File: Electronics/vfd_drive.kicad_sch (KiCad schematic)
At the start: 3 parts, among them J6 Conn_01x08_Pin, U3 74HC595, U4 TBD62783A

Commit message: Added filament timer
Added a timer to control the filament h-brdige on the main PCB.
Also added some more decoupling capacitors, but some have dubious
placement. Still better than nothing.
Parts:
- added C13: 100n, Capacitor_THT:C_Disc_D5.1mm_W3.2mm_P5.00mm, symbol Device:C
- renumbered U3 to U4, U4 to U5
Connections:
- net GND: now also C13.2
- net LOGIC_VCC: now also C13.1
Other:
- note added: "Decoupling"

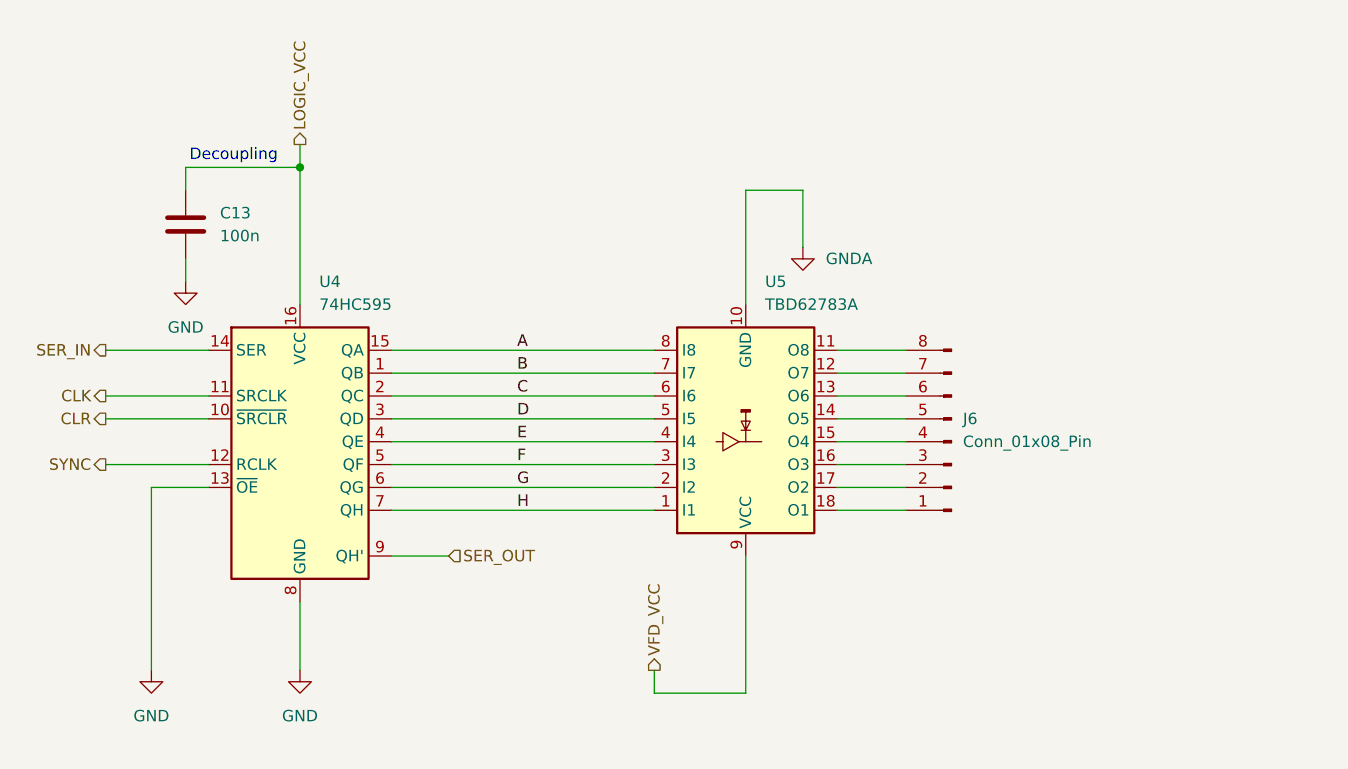
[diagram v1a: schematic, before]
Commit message: Added VFD output pulldowns
Added pulldowns and more decoupling capacitors. The capacitors and
pulldowns can probably be omitted, but I've put them in for more flexibility.
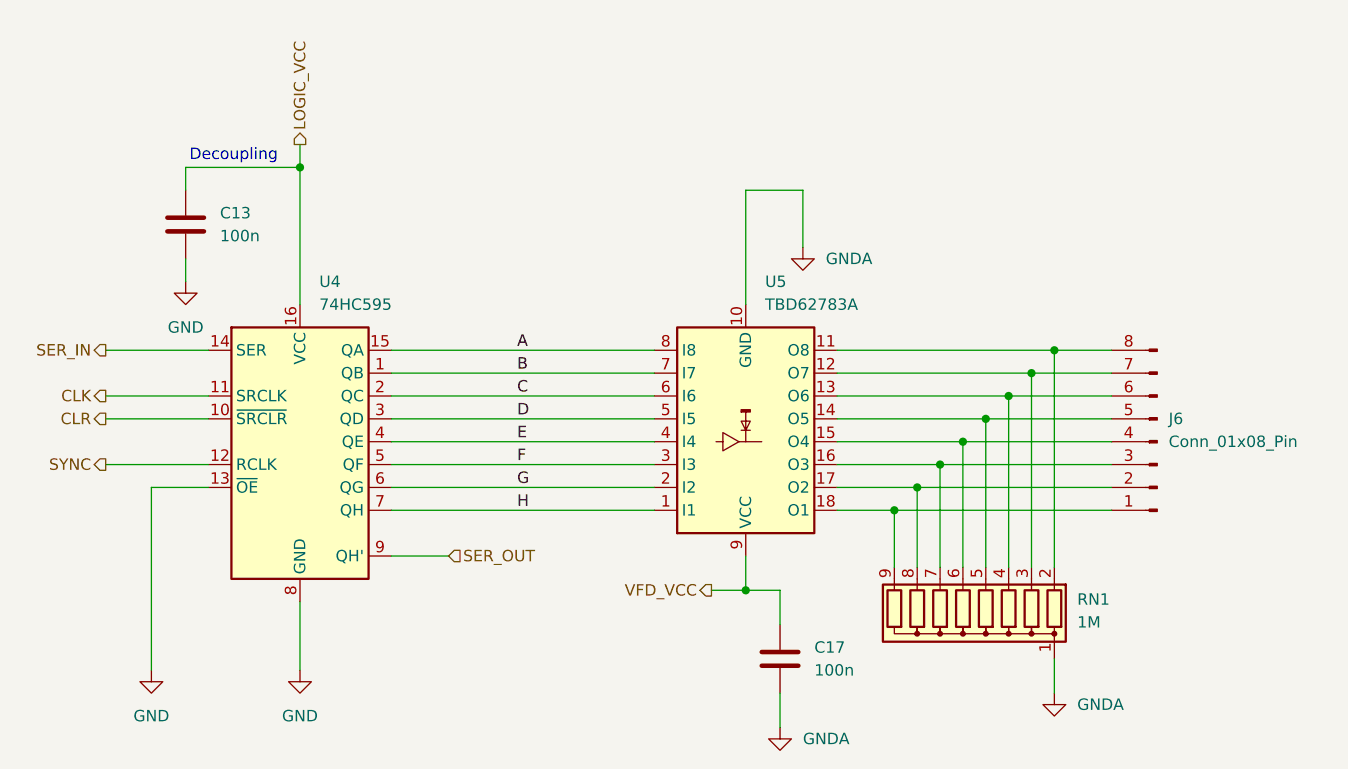
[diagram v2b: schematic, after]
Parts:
- added C17: 100n, Capacitor_THT:C_Disc_D5.1mm_W3.2mm_P5.00mm, symbol Device:C
- added RN1: 1M, Resistor_THT:R_Array_SIP9, symbol Device:R_Network08
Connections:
- net GNDA: now also C17.2, RN1.1 (common)
- net VFD_VCC: now also C17.1
- net at J6.8 (Pin_8), U5.11 (O8): now also RN1.2 (R1)
- net at J6.7 (Pin_7), U5.12 (O7): now also RN1.3 (R2)
- net at J6.6 (Pin_6), U5.13 (O6): now also RN1.4 (R3)
- net at J6.5 (Pin_5), U5.14 (O5): now also RN1.5 (R4)
- net at J6.4 (Pin_4), U5.15 (O4): now also RN1.6 (R5)
- net at J6.3 (Pin_3), U5.16 (O3): now also RN1.7 (R6)
- net at J6.2 (Pin_2), U5.17 (O2): now also RN1.8 (R7)
- net at J6.1 (Pin_1), U5.18 (O1): now also RN1.9 (R8)
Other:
- moved on the sheet: J6

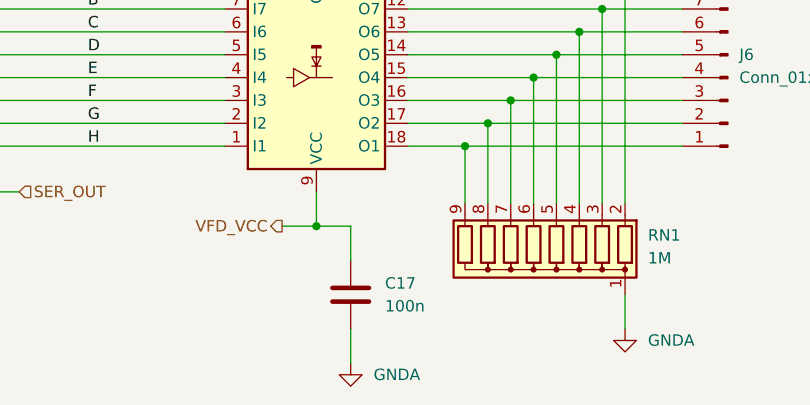
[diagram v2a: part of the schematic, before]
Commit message: Fixed H-bridge
Old H-bridge was the wrong type, changed to using some P-channel
mosfets. Also fixed the cost spreadsheet.
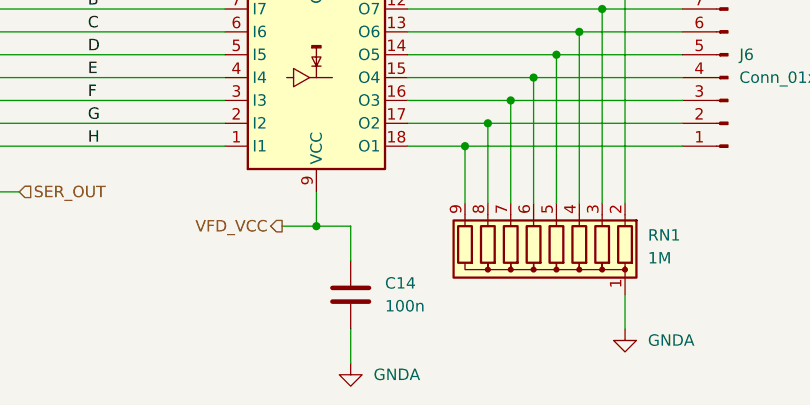
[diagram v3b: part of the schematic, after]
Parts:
- renumbered C17 to C14
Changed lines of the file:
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@@
 			(project "vfd"
 				(path "/36e0811c-69c7-4576-98bb-165d7651c83d/27d484a1-8c30-4726-b590-26be001e1b89"
-					(reference "#PWR082")
-					(unit 1)
-				)
-				(path "/36e0811c-69c7-4576-98bb-165d7651c83d/4abe82bf-2397-47f3-bdf5-0f85616bed30"
 					(reference "#PWR086")
 					(unit 1)
 				)
+				(path "/36e0811c-69c7-4576-98bb-165d7651c83d/4abe82bf-2397-47f3-bdf5-0f85616bed30"
+					(reference "#PWR092")
+					(unit 1)
+				)
 				(path "/36e0811c-69c7-4576-98bb-165d7651c83d/64881d92-68ba-4505-901e-5a279b3a305e"
 					(reference "#PWR074")
@@
 				)
 				(path "/36e0811c-69c7-4576-98bb-165d7651c83d/dcab1e90-0fd0-4de9-948e-22e325fd164f"
-					(reference "#PWR078")
+					(reference "#PWR080")
 					(unit 1)
 				)
@@
 			(project "vfd"
 				(path "/36e0811c-69c7-4576-98bb-165d7651c83d/27d484a1-8c30-4726-b590-26be001e1b89"
-					(reference "#PWR085")
-					(unit 1)
-				)
-				(path "/36e0811c-69c7-4576-98bb-165d7651c83d/4abe82bf-2397-47f3-bdf5-0f85616bed30"
 					(reference "#PWR089")
 					(unit 1)
 				)
+				(path "/36e0811c-69c7-4576-98bb-165d7651c83d/4abe82bf-2397-47f3-bdf5-0f85616bed30"
+					(reference "#PWR095")
+					(unit 1)
+				)
 				(path "/36e0811c-69c7-4576-98bb-165d7651c83d/64881d92-68ba-4505-901e-5a279b3a305e"
 					(reference "#PWR077")
@@
 				)
 				(path "/36e0811c-69c7-4576-98bb-165d7651c83d/dcab1e90-0fd0-4de9-948e-22e325fd164f"
-					(reference "#PWR081")
+					(reference "#PWR083")
 					(unit 1)
 				)
@@
 		(dnp no)
 		(fields_autoplaced yes)
-		(property "Reference" "#PWR090"
+		(property "Reference" "#PWR078"
 			(at 162.56 92.71 0)
 			(effects
@@
 			(project "vvfd"
 				(path "/36e0811c-69c7-4576-98bb-165d7651c83d/27d484a1-8c30-4726-b590-26be001e1b89"
-					(reference "#PWR092")
-					(unit 1)
-				)
-				(path "/36e0811c-69c7-4576-98bb-165d7651c83d/4abe82bf-2397-47f3-bdf5-0f85616bed30"
-					(reference "#PWR093")
-					(unit 1)
-				)
-				(path "/36e0811c-69c7-4576-98bb-165d7651c83d/64881d92-68ba-4505-901e-5a279b3a305e"
 					(reference "#PWR090")
 					(unit 1)
 				)
-				(path "/36e0811c-69c7-4576-98bb-165d7651c83d/dcab1e90-0fd0-4de9-948e-22e325fd164f"
-					(reference "#PWR091")
+				(path "/36e0811c-69c7-4576-98bb-165d7651c83d/4abe82bf-2397-47f3-bdf5-0f85616bed30"
+					(reference "#PWR096")
+					(unit 1)
+				)
+				(path "/36e0811c-69c7-4576-98bb-165d7651c83d/64881d92-68ba-4505-901e-5a279b3a305e"
+					(reference "#PWR078")
+					(unit 1)
+				)
+				(path "/36e0811c-69c7-4576-98bb-165d7651c83d/dcab1e90-0fd0-4de9-948e-22e325fd164f"
+					(reference "#PWR084")
 					(unit 1)
 				)
@@
 			(project "vvfd"
 				(path "/36e0811c-69c7-4576-98bb-165d7651c83d/27d484a1-8c30-4726-b590-26be001e1b89"
+					(reference "C17")
+					(unit 1)
+				)
+				(path "/36e0811c-69c7-4576-98bb-165d7651c83d/4abe82bf-2397-47f3-bdf5-0f85616bed30"
+					(reference "C19")
+					(unit 1)
+				)
+				(path "/36e0811c-69c7-4576-98bb-165d7651c83d/64881d92-68ba-4505-901e-5a279b3a305e"
+					(reference "C13")
+					(unit 1)
+				)
+				(path "/36e0811c-69c7-4576-98bb-165d7651c83d/dcab1e90-0fd0-4de9-948e-22e325fd164f"
 					(reference "C15")
-					(unit 1)
-				)
-				(path "/36e0811c-69c7-4576-98bb-165d7651c83d/4abe82bf-2397-47f3-bdf5-0f85616bed30"
-					(reference "C16")
-					(unit 1)
-				)
-				(path "/36e0811c-69c7-4576-98bb-165d7651c83d/64881d92-68ba-4505-901e-5a279b3a305e"
-					(reference "C13")
-					(unit 1)
-				)
-				(path "/36e0811c-69c7-4576-98bb-165d7651c83d/dcab1e90-0fd0-4de9-948e-22e325fd164f"
-					(reference "C14")
 					(unit 1)
 				)
@@
 		(dnp no)
 		(fields_autoplaced yes)
-		(property "Reference" "#PWR094"
+		(property "Reference" "#PWR079"
 			(at 132.08 96.52 0)
 			(effects
@@
 			(project "vvfd"
 				(path "/36e0811c-69c7-4576-98bb-165d7651c83d/27d484a1-8c30-4726-b590-26be001e1b89"
-					(reference "#PWR096")
+					(reference "#PWR091")
 					(unit 1)
 				)
@@
 				)
 				(path "/36e0811c-69c7-4576-98bb-165d7651c83d/64881d92-68ba-4505-901e-5a279b3a305e"
-					(reference "#PWR094")
-					(unit 1)
-				)
-				(path "/36e0811c-69c7-4576-98bb-165d7651c83d/dcab1e90-0fd0-4de9-948e-22e325fd164f"
-					(reference "#PWR095")
+					(reference "#PWR079")
+					(unit 1)
+				)
+				(path "/36e0811c-69c7-4576-98bb-165d7651c83d/dcab1e90-0fd0-4de9-948e-22e325fd164f"
+					(reference "#PWR085")
 					(unit 1)
 				)
@@
 			(project "vfd"
 				(path "/36e0811c-69c7-4576-98bb-165d7651c83d/27d484a1-8c30-4726-b590-26be001e1b89"
-					(reference "#PWR084")
-					(unit 1)
-				)
-				(path "/36e0811c-69c7-4576-98bb-165d7651c83d/4abe82bf-2397-47f3-bdf5-0f85616bed30"
 					(reference "#PWR088")
 					(unit 1)
 				)
+				(path "/36e0811c-69c7-4576-98bb-165d7651c83d/4abe82bf-2397-47f3-bdf5-0f85616bed30"
+					(reference "#PWR094")
+					(unit 1)
+				)
 				(path "/36e0811c-69c7-4576-98bb-165d7651c83d/64881d92-68ba-4505-901e-5a279b3a305e"
 					(reference "#PWR076")
@@
 				)
 				(path "/36e0811c-69c7-4576-98bb-165d7651c83d/dcab1e90-0fd0-4de9-948e-22e325fd164f"
-					(reference "#PWR080")
+					(reference "#PWR082")
 					(unit 1)
 				)
@@
 		(dnp no)
 		(fields_autoplaced yes)
-		(property "Reference" "C17"
+		(property "Reference" "C14"
 			(at 135.89 81.2799 0)
 			(effects
@@
 			(project "vvfd"
 				(path "/36e0811c-69c7-4576-98bb-165d7651c83d/27d484a1-8c30-4726-b590-26be001e1b89"
-					(reference "C19")
+					(reference "C18")
 					(unit 1)
 				)
@@
 				)
 				(path "/36e0811c-69c7-4576-98bb-165d7651c83d/64881d92-68ba-4505-901e-5a279b3a305e"
-					(reference "C17")
-					(unit 1)
-				)
-				(path "/36e0811c-69c7-4576-98bb-165d7651c83d/dcab1e90-0fd0-4de9-948e-22e325fd164f"
-					(reference "C18")
+					(reference "C14")
+					(unit 1)
+				)
+				(path "/36e0811c-69c7-4576-98bb-165d7651c83d/dcab1e90-0fd0-4de9-948e-22e325fd164f"
+					(reference "C16")
 					(unit 1)
 				)
@@
 			(project "vvfd"
 				(path "/36e0811c-69c7-4576-98bb-165d7651c83d/27d484a1-8c30-4726-b590-26be001e1b89"
-					(reference "#PWR083")
-					(unit 1)
-				)
-				(path "/36e0811c-69c7-4576-98bb-165d7651c83d/4abe82bf-2397-47f3-bdf5-0f85616bed30"
 					(reference "#PWR087")
 					(unit 1)
 				)
+				(path "/36e0811c-69c7-4576-98bb-165d7651c83d/4abe82bf-2397-47f3-bdf5-0f85616bed30"
+					(reference "#PWR093")
+					(unit 1)
+				)
 				(path "/36e0811c-69c7-4576-98bb-165d7651c83d/64881d92-68ba-4505-901e-5a279b3a305e"
 					(reference "#PWR075")
@@
 				)
 				(path "/36e0811c-69c7-4576-98bb-165d7651c83d/dcab1e90-0fd0-4de9-948e-22e325fd164f"
-					(reference "#PWR079")
-					(unit 1)
-				)
+					(reference "#PWR081")
+					(unit 1)
+				)

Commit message: Updated BOM
Updated BOMs because some of the component prices changed and a part
went out of stock.
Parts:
- U5: footprint Custom:SOP-18_7.495x11.515mm_P1.27mm -> Package_SO:SOP-18_7x12.5mm_P1.27mm; Digikey Part No TBD62783AFWGELCT-ND -> TBD62783AFGELCT-ND; Manufacturer Part No TBD62783AFWG,EL -> TBD62783AFG,EL; Unit Price ($) 3.36950 -> 4.87600
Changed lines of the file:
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@@
 			)
 		)
-		(property "Footprint" "Custom:SOP-18_7.495x11.515mm_P1.27mm"
+		(property "Footprint" "Package_SO:SOP-18_7x12.5mm_P1.27mm"
 			(at 128.27 44.45 0)
 			(effects
@@
 			)
 		)
-		(property "Digikey Part No" "TBD62783AFWGELCT-ND"
+		(property "Digikey Part No" "TBD62783AFGELCT-ND"
 			(at 128.27 58.42 0)
 			(effects
@@
 			)
 		)
-		(property "Manufacturer Part No" "TBD62783AFWG,EL"
+		(property "Manufacturer Part No" "TBD62783AFG,EL"
 			(at 128.27 58.42 0)
 			(effects
@@
 			)
 		)
-		(property "Unit Price ($)" "3.36950"
+		(property "Unit Price ($)" "4.87600"
 			(at 128.27 58.42 0)
 			(effects
